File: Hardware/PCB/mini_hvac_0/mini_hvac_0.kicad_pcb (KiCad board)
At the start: 2 copper layers, 150 x 85 mm, 25 parts, among them J1 Conn_01x03_Pin, J10 Conn_01x03_Pin, J11 Conn_01x03_Pin, J12 Conn_01x03_Pin, J13 Conn_01x03_Pin, J14 Conn_01x04_Pin, J15 Conn_01x04_Socket, J2 Conn_01x03_Pin, J20 Conn_01x06_Socket, J3 Conn_01x03_Pin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

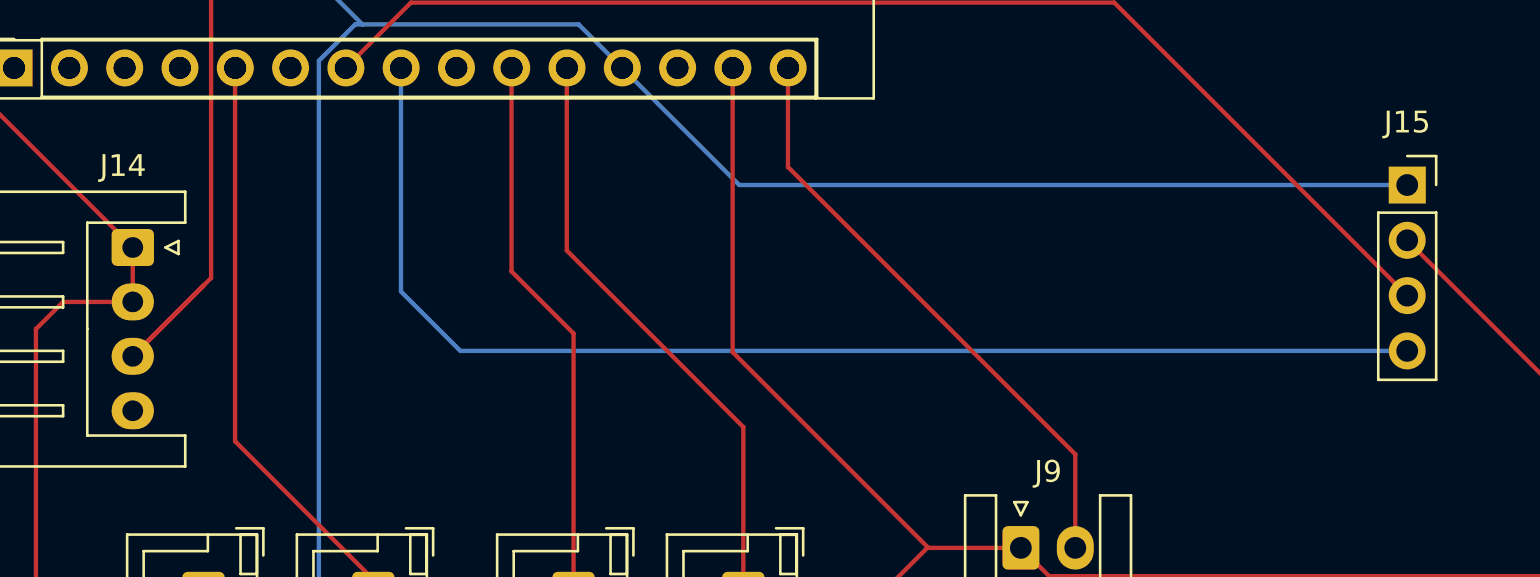
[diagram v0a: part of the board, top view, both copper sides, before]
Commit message: routed power selector and generated BoM
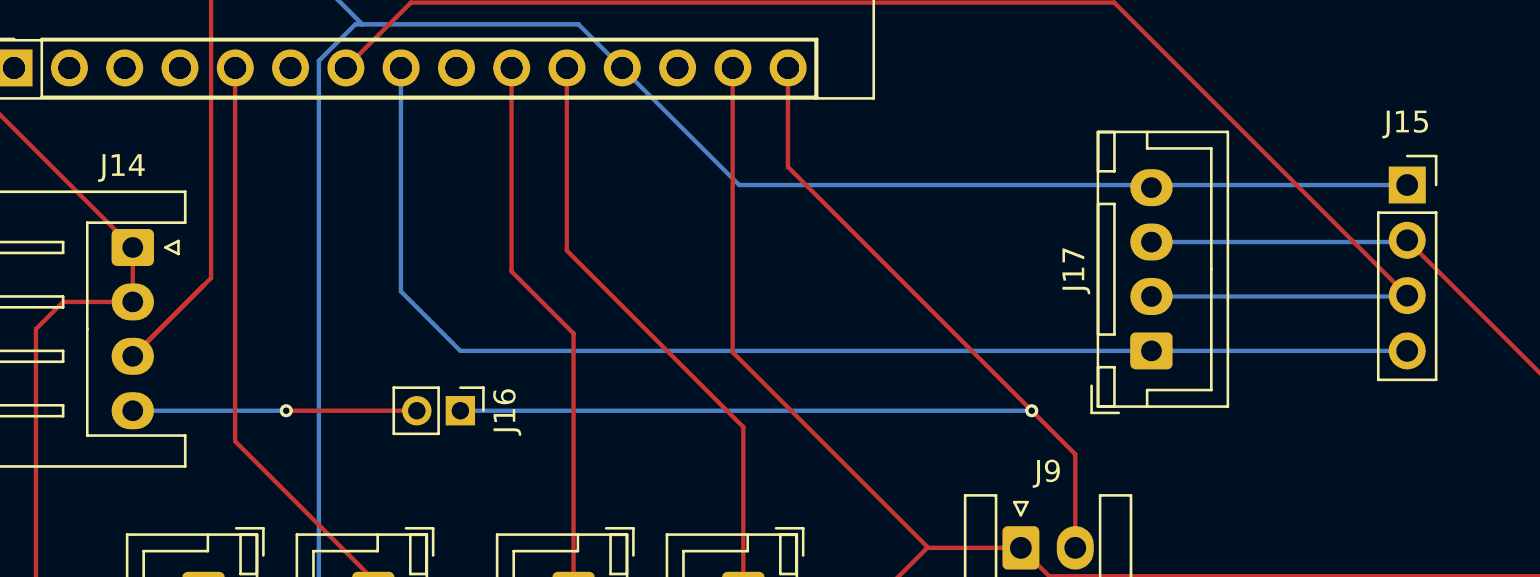
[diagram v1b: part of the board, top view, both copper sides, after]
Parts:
- added J16: Conn_01x02_Pin, Connector_PinHeader_2.00mm:PinHeader_1x02_P2.00mm_Vertical, F.Cu at (127.5, 141.2)
- added J17: Conn_01x04_Pin, Connector_JST:JST_XH_B4B-XH-A_1x04_P2.50mm_Vertical, F.Cu at (159.2, 138.5)
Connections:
- J14 pad 4: unconnected-(J14-Pin_4-Pad4) -> CD_PS
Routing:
- net VIN: track 27.5 -> 53.8 mm, vias 0 -> 1
- net CD_PS: track 0.00 -> 13.0 mm, vias 0 -> 1
- net GND: track 323.1 -> 334.8 mm
- net A3: track 55.6 -> 67.4 mm

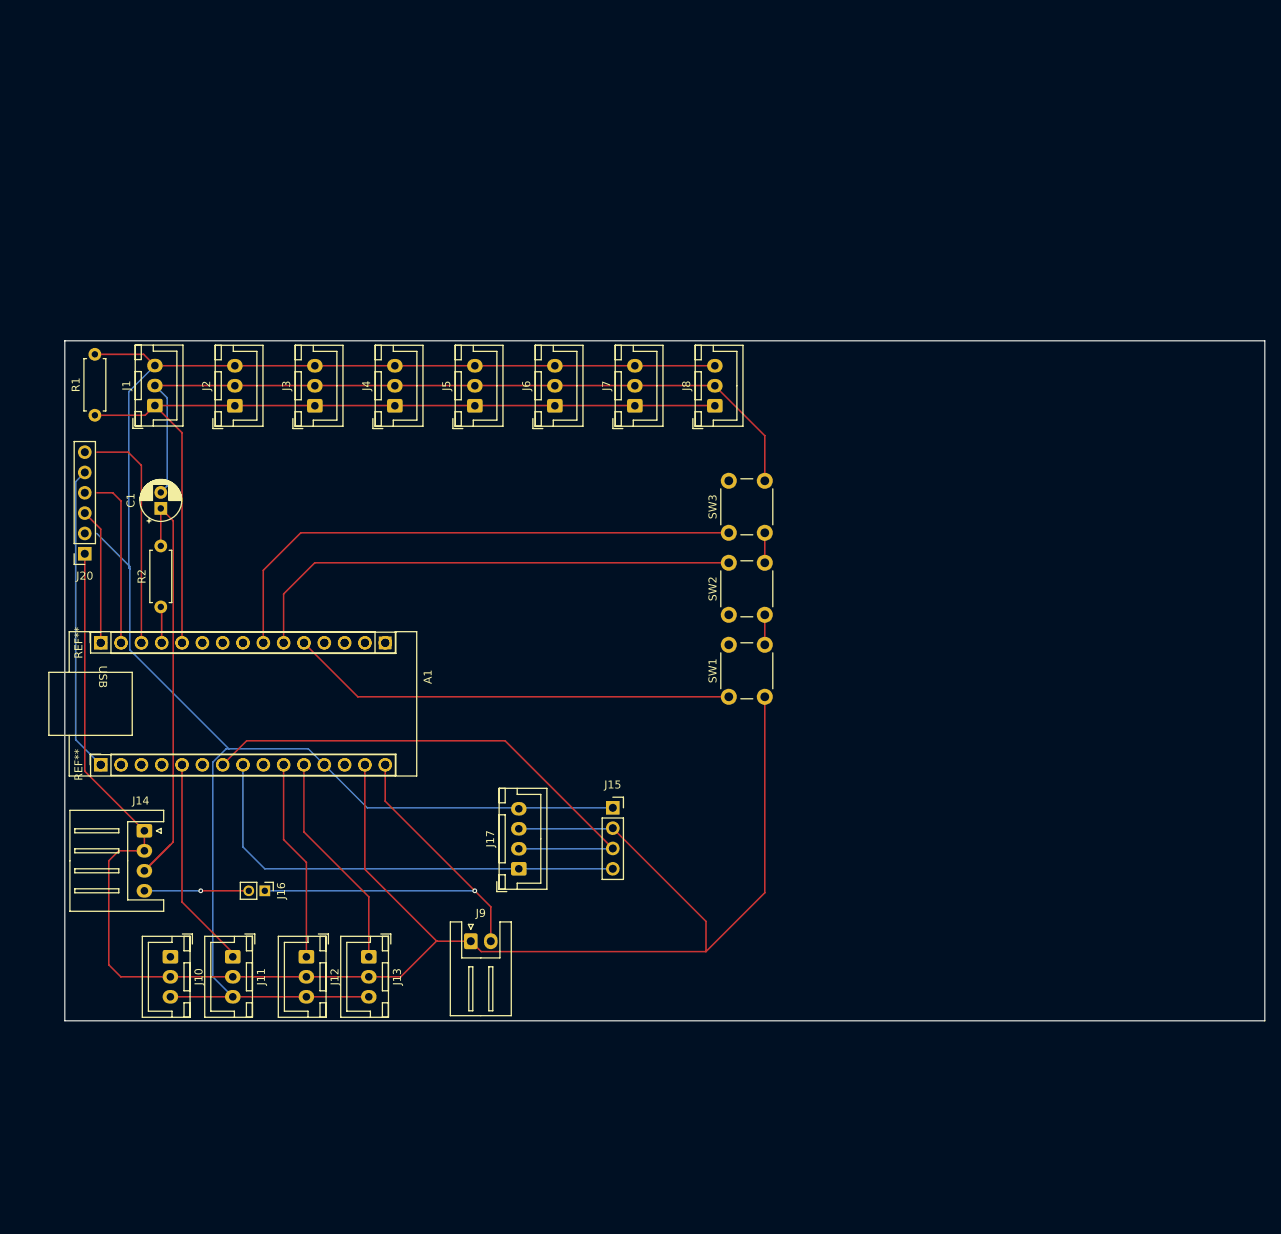
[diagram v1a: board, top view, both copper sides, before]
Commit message: new PCB layout
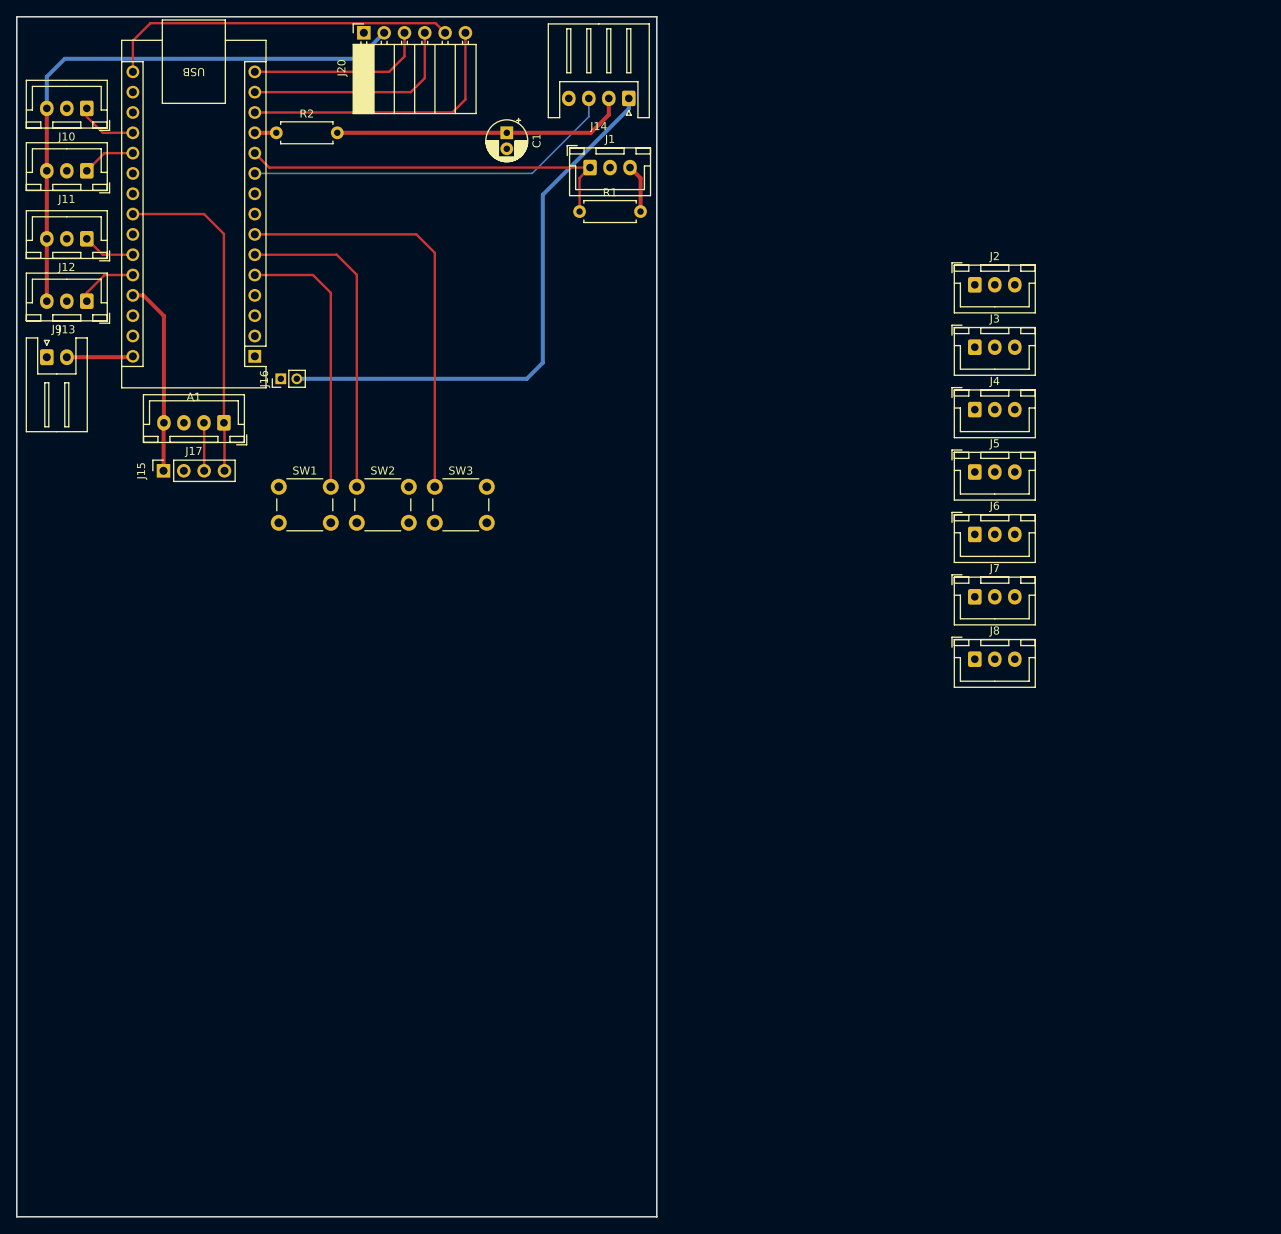
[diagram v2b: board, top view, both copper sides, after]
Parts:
- removed REF** (x2): PinSocket_1x15_P2.54mm_Vertical, Connector_PinSocket_2.54mm:PinSocket_1x15_P2.54mm_Vertical
- J20: footprint Connector_PinSocket_2.54mm:PinSocket_1x06_P2.54mm_Vertical -> Connector_PinSocket_2.54mm:PinSocket_1x06_P2.54mm_Horizontal
- moved J14 109.8 mm to (173.0, 42.2), turned to 180 degrees
- moved J10 106.6 mm to (105.2, 43.5), turned to 180 degrees
- moved J11 99.9 mm to (105.2, 51.2), turned to 180 degrees
- moved J12 93.9 mm to (105.2, 59.8), turned to 180 degrees
- moved J2 93.7 mm to (216.2, 65.5), turned to 0 degrees
- moved J9 90.2 mm to (100.2, 74.5)
- moved J13 89.2 mm to (105.2, 67.5), turned to 180 degrees
- moved J3 82.8 mm to (216.2, 73.3), turned to 0 degrees
- moved J20 73.9 mm to (139.9, 34.0), turned to 90 degrees
- moved J4 72.5 mm to (216.2, 81.1), turned to 0 degrees
- moved J15 70.2 mm to (114.8, 88.8), turned to 90 degrees
- moved J17 66.8 mm to (122.4, 82.8), turned to 180 degrees
- moved R1 65.7 mm to (166.8, 56.3), turned to 0 degrees
- moved J16 64.0 mm to (129.5, 77.2), turned to 90 degrees
- moved C1 63.8 mm to (157.8, 46.5), turned to -90 degrees
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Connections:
- A1 pad 10: unconnected-(A1-D7-Pad10) -> CD_EN
- C1 pad 1: Net-(J14-Pin_3) -> Net-(J14-Pin_2)
- J14 pad 1: GND -> CD_PS
- J14 pad 2: GND -> Net-(J14-Pin_2)
- J14 pad 3: Net-(J14-Pin_3) -> CD_EN
- J14 pad 4: CD_PS -> GND
- R2 pad 2: Net-(J14-Pin_3) -> Net-(J14-Pin_2)
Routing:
- net GND: track 334.8 -> 0.00 mm
- net +5V: track 247.6 -> 102.9 mm
- net A3: track 67.4 -> 6.01 mm
- net D8: track 109.1 -> 48.7 mm
- net Net-(J14-Pin_3): track 56.7 -> 0.00 mm
- net CD_PS: track 13.0 -> 69.1 mm, vias 1 -> 0
- net CD_EN: track 0.00 -> 47.0 mm
- net VIN: track 53.8 -> 8.31 mm, vias 1 -> 0
- net Net-(J14-Pin_2): track 0.00 -> 36.4 mm
- net D3: track 63.4 -> 40.3 mm
- net D2: track 55.9 -> 34.7 mm
- net A1: track 26.6 -> 6.68 mm
- net A7: track 27.4 -> 7.73 mm
- net A6: track 25.2 -> 6.58 mm
- net D4: track 69.2 -> 52.7 mm
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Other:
- board size 150 x 85 mm -> 80 x 150 mm

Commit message: even smaller layout, horizontal footprints replaced with vertical and orientation changed
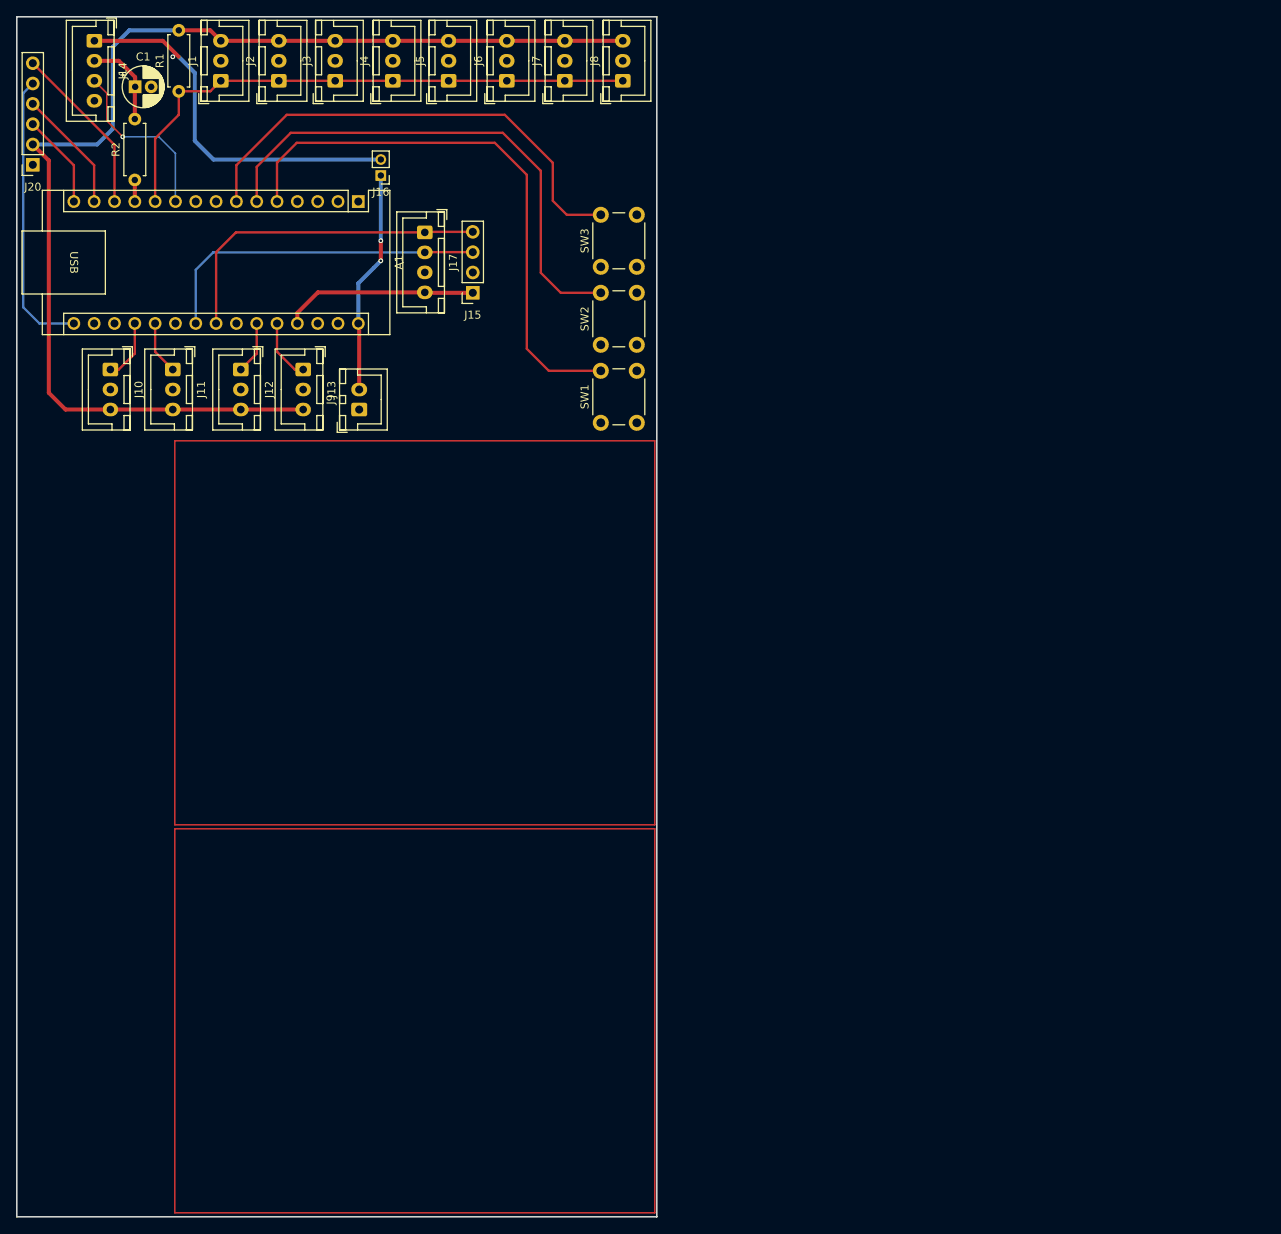
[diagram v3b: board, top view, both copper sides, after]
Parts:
- J14: footprint Connector_JST:JST_XH_S4B-XH-A_1x04_P2.50mm_Horizontal -> Connector_JST:JST_XH_B4B-XH-A_1x04_P2.50mm_Vertical
- J20: footprint Connector_PinSocket_2.54mm:PinSocket_1x06_P2.54mm_Horizontal -> Connector_PinSocket_2.54mm:PinSocket_1x06_P2.54mm_Vertical
- J9: footprint Connector_JST:JST_XH_S2B-XH-A_1x02_P2.50mm_Horizontal -> Connector_JST:JST_XH_B2B-XH-A_1x02_P2.50mm_Vertical
- moved J2 90.7 mm to (129.2, 40.0), turned to 90 degrees
- moved J3 86.6 mm to (136.3, 40.0), turned to 90 degrees
- moved J8 84.6 mm to (172.2, 40.0), turned to 90 degrees
- moved J4 83.6 mm to (143.5, 40.0), turned to 90 degrees
- moved J7 82.4 mm to (165.0, 40.0), turned to 90 degrees
- moved J5 82.0 mm to (150.5, 40.0), turned to 90 degrees
- moved J6 81.5 mm to (157.8, 40.0), turned to 90 degrees
- moved J14 67.2 mm to (106.2, 35.0), turned to -90 degrees
- moved R1 52.3 mm to (116.8, 41.3), turned to 90 degrees
- moved J1 47.4 mm to (122.0, 40.0), turned to 90 degrees
- moved C1 46.8 mm to (111.3, 40.8), turned to 0 degrees
- moved J15 44.6 mm to (153.5, 66.5), turned to 180 degrees
- moved J20 44.5 mm to (98.5, 50.5), turned to 180 degrees
- moved SW1 41.0 mm to (169.5, 82.8), turned to 90 degrees
- moved J9 39.6 mm to (139.3, 81.1), turned to 90 degrees
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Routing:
- net +5V: track 102.9 -> 175.1 mm
- net D2: track 34.7 -> 70.9 mm
- net A3: track 6.01 -> 42.2 mm
- net Net-(J14-Pin_2): track 36.4 -> 11.2 mm
- net CD_EN: track 47.0 -> 21.9 mm, vias 0 -> 1
- net D3: track 40.3 -> 64.9 mm
- net D8: track 48.7 -> 71.0 mm
- net CD_PS: track 69.1 -> 46.9 mm, vias 0 -> 1
- net VIN: track 8.31 -> 28.0 mm, vias 0 -> 2
- net D10: track 35.3 -> 21.5 mm
- net D11/MOSI: track 27.6 -> 15.4 mm
- net D12/MISO: track 22.5 -> 11.8 mm
- net D13/SCK: track 44.3 -> 35.6 mm
- net D4: track 52.7 -> 60.7 mm
